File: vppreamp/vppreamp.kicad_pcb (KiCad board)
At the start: 2 copper layers, 24 parts, among them J1 Input, J2 Output, SW1 On, U1 TL072

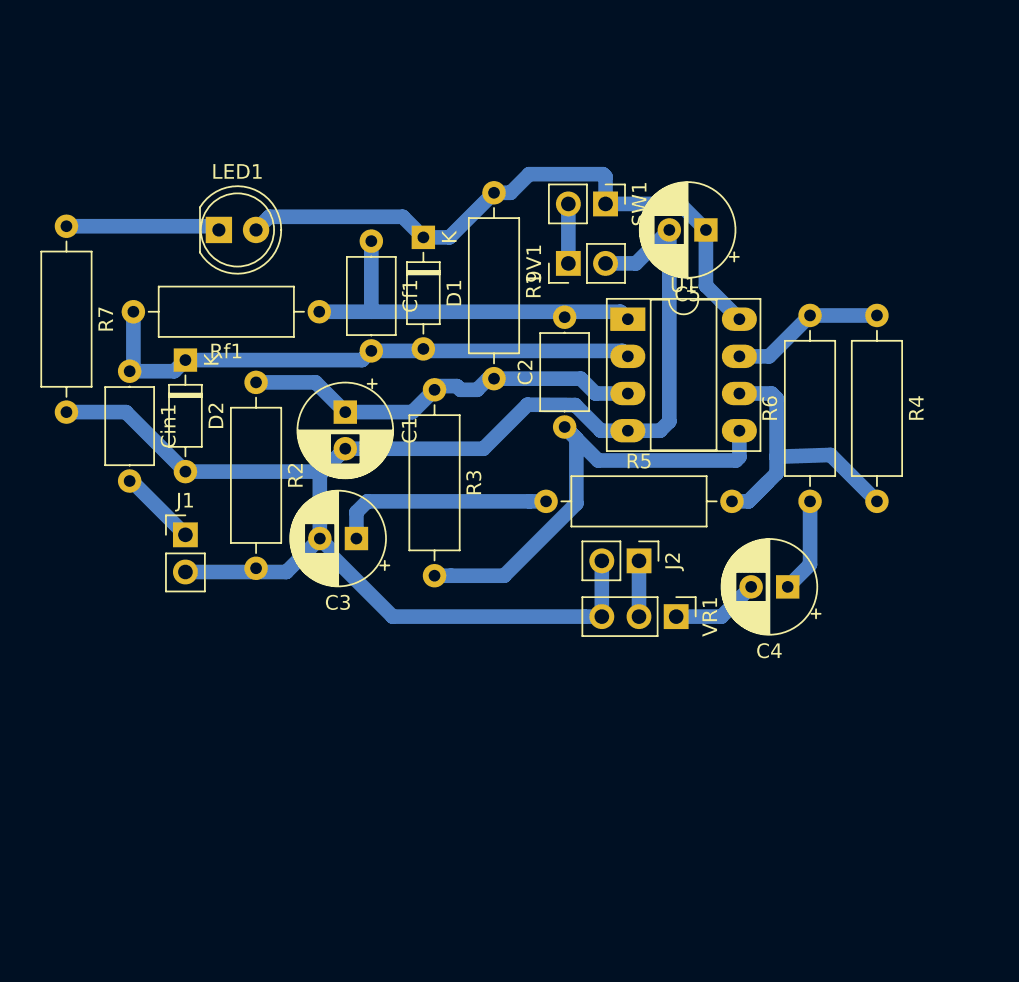
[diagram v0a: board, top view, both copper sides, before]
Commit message: added ground plane, bits of labeling
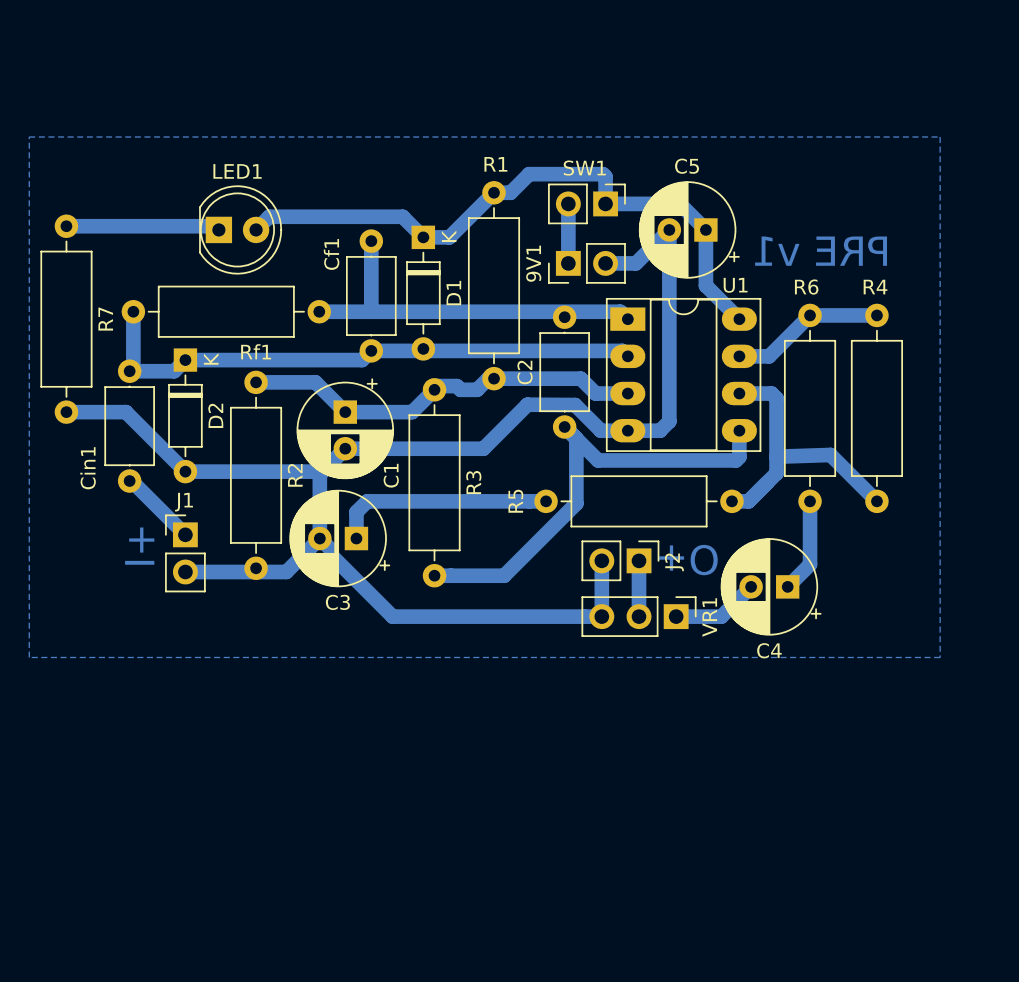
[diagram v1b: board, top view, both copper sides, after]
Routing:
- added copper zone on B.Cu, net GND
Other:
- board text added: "+I"
- board text added: "+O"
- board text added: "PRE v1"

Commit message: added power jack
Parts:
- added J3: Barrel_Jack_Switch, Connector_BarrelJack:BarrelJack_Horizontal, F.Cu at (184.5, 42.2)
- moved 9V1 7.22 mm to (166.4, 35.8), turned to 270 degrees
- moved SW1 3.74 mm to (166.5, 42.4), turned to 180 degrees
- moved C5 2.44 mm to (172.1, 41.0), turned to 0 degrees
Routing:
- net GND: track 106.6 -> 85.1 mm
- net Net-(9V1-Pad1): track 4.06 -> 22.4 mm
- net Net-(C5-Pad1): track 43.2 -> 40.6 mm

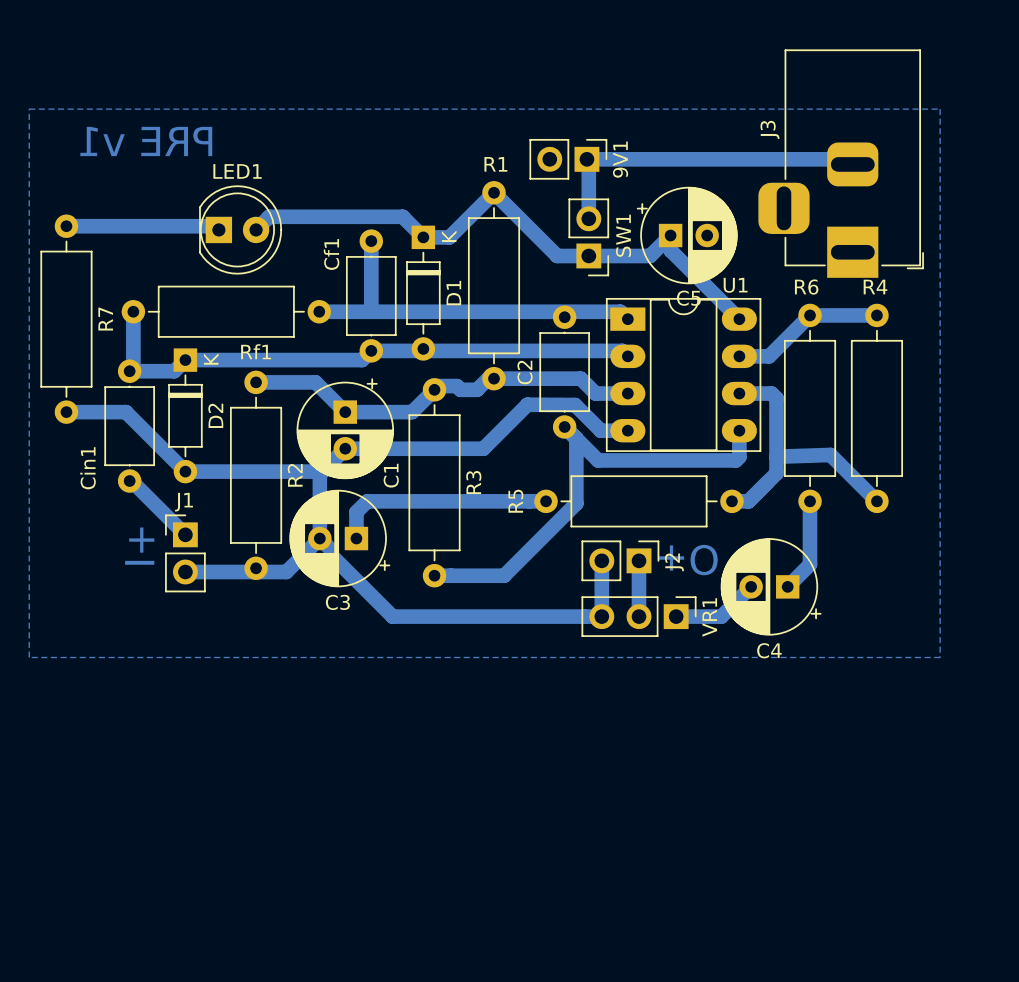
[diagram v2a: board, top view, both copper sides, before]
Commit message: add jacks, remap for v2
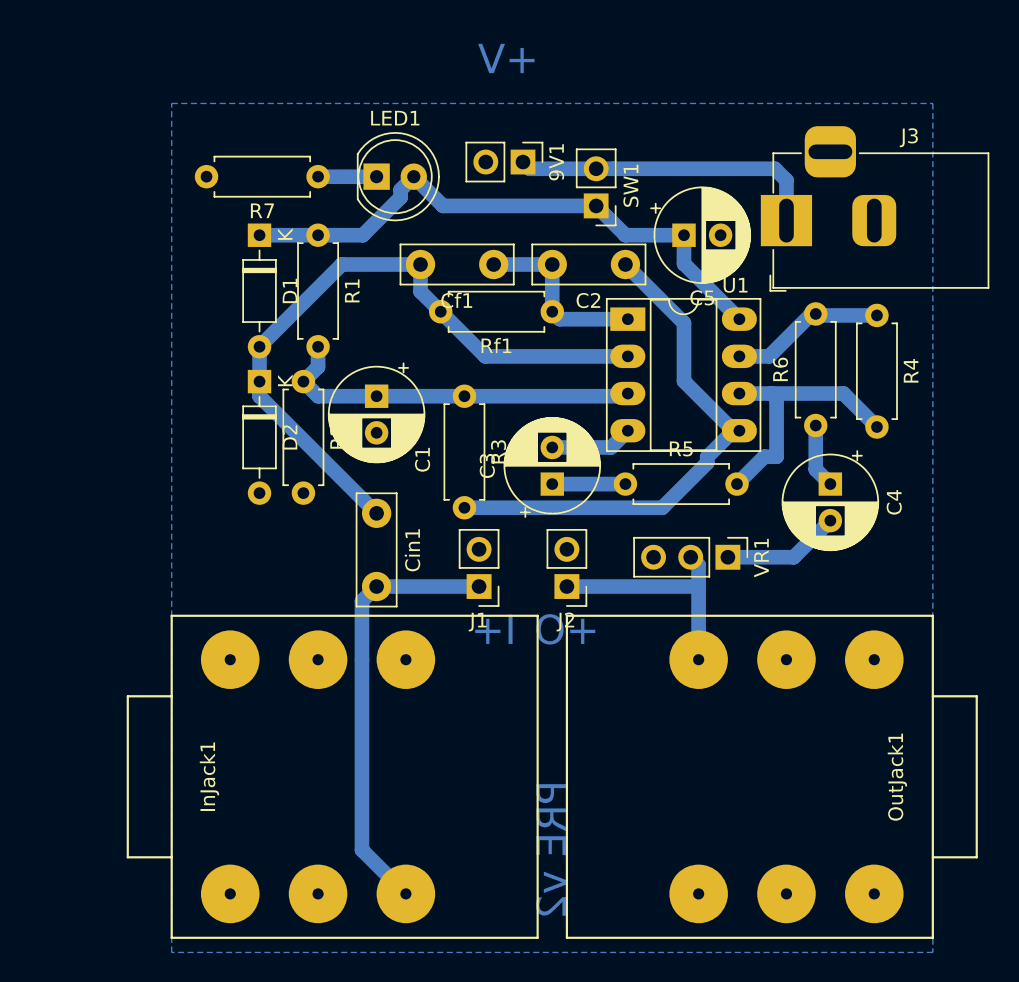
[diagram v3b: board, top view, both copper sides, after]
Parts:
- added InJack1: InJack, NateLibrary:StereoJackTRS3, F.Cu at (140.0, 78.0)
- added OutJack1: OutJack, NateLibrary:StereoJackTRS3, F.Cu at (188.0, 78.0)
- C2, Cf1, Cin1: footprint Capacitor_THT:C_Axial_L5.1mm_D3.1mm_P7.50mm_Horizontal -> Capacitor_THT:C_Disc_D7.5mm_W2.5mm_P5.00mm
- R1, R2, R3, R4, R5, R6, R7, Rf1: footprint Resistor_THT:R_Axial_DIN0309_L9.0mm_D3.2mm_P12.70mm_Horizontal -> Resistor_THT:R_Axial_DIN0207_L6.3mm_D2.5mm_P7.62mm_Horizontal
- moved J1 20.4 mm to (159.0, 65.0), turned to 180 degrees
- moved Cin1 19.5 mm to (152.0, 60.0)
- moved R7 17.5 mm to (148.0, 37.0), turned to 180 degrees
- moved Rf1 15.9 mm to (164.0, 46.2)
- moved C3 13.9 mm to (164.0, 58.0), turned to 90 degrees
- moved R1 12.4 mm to (148.0, 41.0)
- moved C2 11.9 mm to (169.0, 43.0), turned to 180 degrees
- moved LED1 11.4 mm to (152.0, 37.0)
- moved D1 11.2 mm to (144.0, 41.0)
- moved Cf1 8.51 mm to (160.0, 43.0), turned to 180 degrees
- moved C4 7.60 mm to (183.0, 58.0), turned to 270 degrees
- moved R5 5.55 mm to (169.0, 58.0)
- moved VR1 5.38 mm to (176.0, 63.0)
- moved D2 5.27 mm to (144.0, 51.0)
- moved J2 5.23 mm to (165.0, 65.0), turned to 180 degrees
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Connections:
- J3 pad 1: GND -> Net-(9V1-Pad1)
- J3 pad 2: Net-(9V1-Pad1) -> GND
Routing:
- net GND: track 85.1 -> 5.64 mm
- net Net-(Cin1-Pad2): track 5.33 -> 29.7 mm
- net Net-(C2-Pad2): track 26.1 -> 13.0 mm
- net Net-(J2-Pad1): track 3.81 -> 16.2 mm
- net Net-(C3-Pad1): track 15.1 -> 5.00 mm
- net Net-(Cf1-Pad2): track 38.9 -> 45.9 mm
- net Net-(LED1-Pad1): track 10.5 -> 4.00 mm
- net Net-(C2-Pad1): track 32.1 -> 35.6 mm
- net Net-(R4-Pad2): track 21.6 -> 18.3 mm
- net Net-(C1-Pad1): track 28.1 -> 25.8 mm
- net Net-(C4-Pad2): track 5.96 -> 8.04 mm
- net Net-(C4-Pad1): track 6.47 -> 4.41 mm
- net Net-(9V1-Pad1): track 22.4 -> 21.3 mm
- net Net-(C5-Pad1): track 40.6 -> 39.9 mm
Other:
- board text added: "+V"
- board text added: "I+"
- board text added: "PRE v2"
- board text removed: "+I"
- board text removed: "PRE v1"

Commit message: added print files
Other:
- board text removed: "+V"
